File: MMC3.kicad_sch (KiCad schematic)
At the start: 18 parts, among them U11 NES-MMC3, U9 IS62C256AL-45TLI

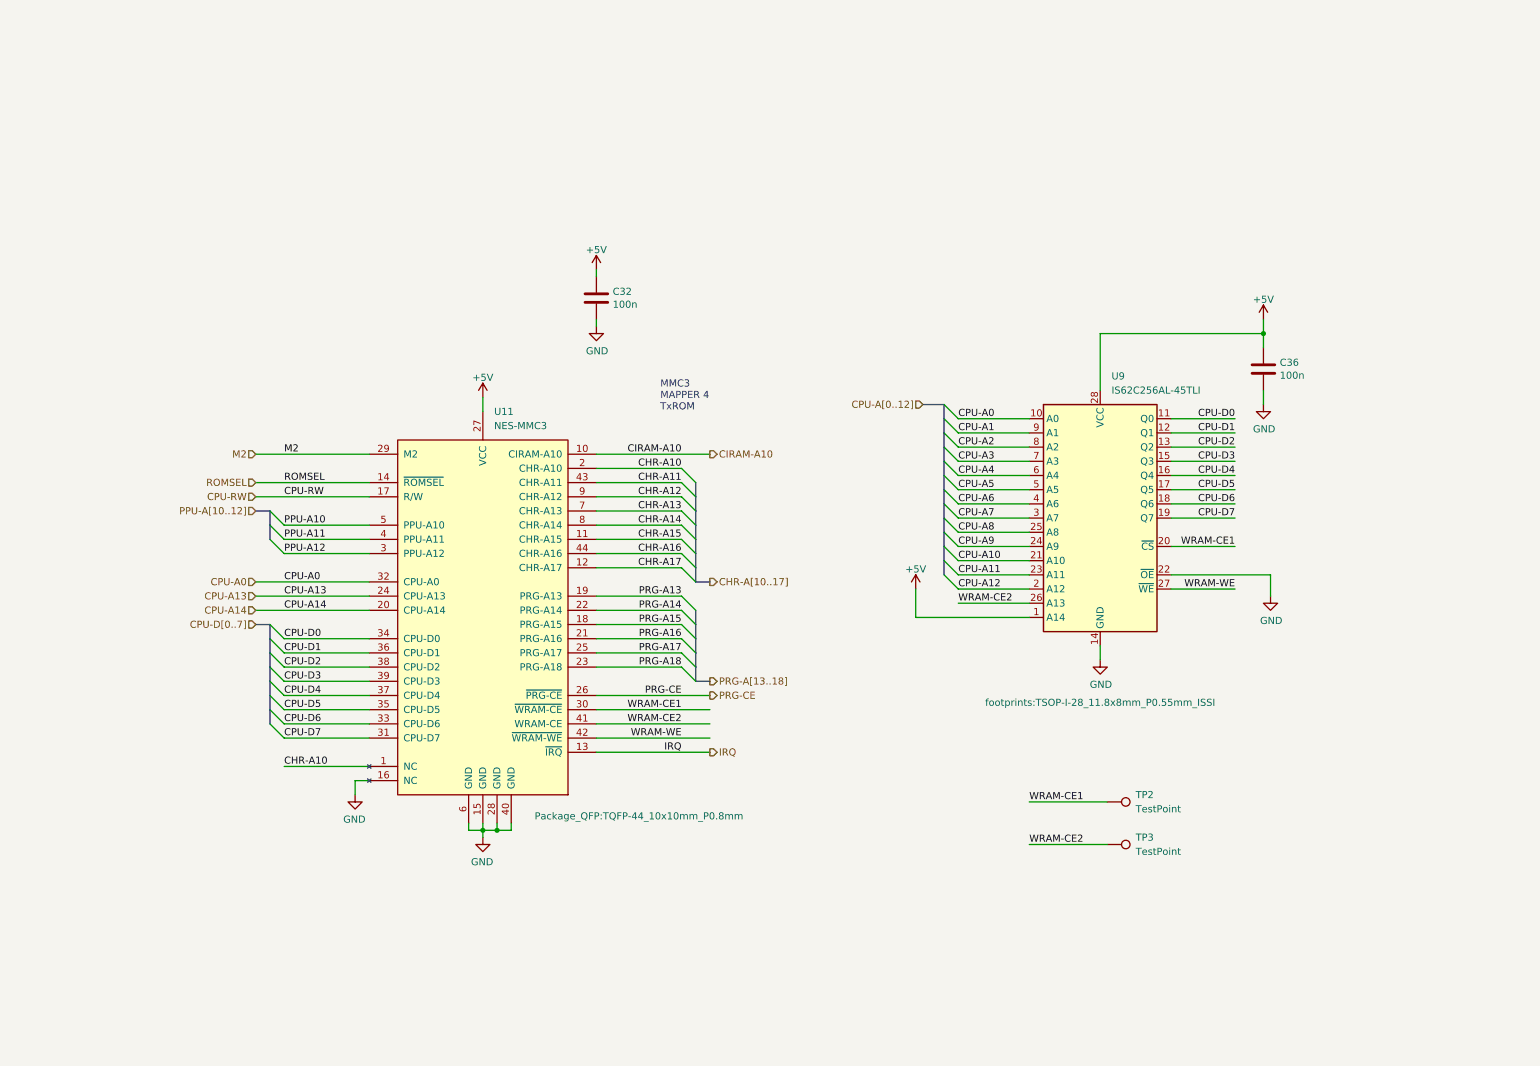
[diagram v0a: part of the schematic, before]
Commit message: rev2 sent to fab
Added CHR RAM.
Changed board to 4 layers (was 2 layers).
Changed passives to 0603 (was 0402)
Fixed CIRAM-A10 not being hooked up
Fixed PPU-A10..A12 being hooked to VRAM but should have been.
Added more silkscreen for easier debugging.
Added filter inductor to 5V from USB-C.
Changed video out to stock (was THS7374)
Changed audio circuit to stock (was headphone amp IC)
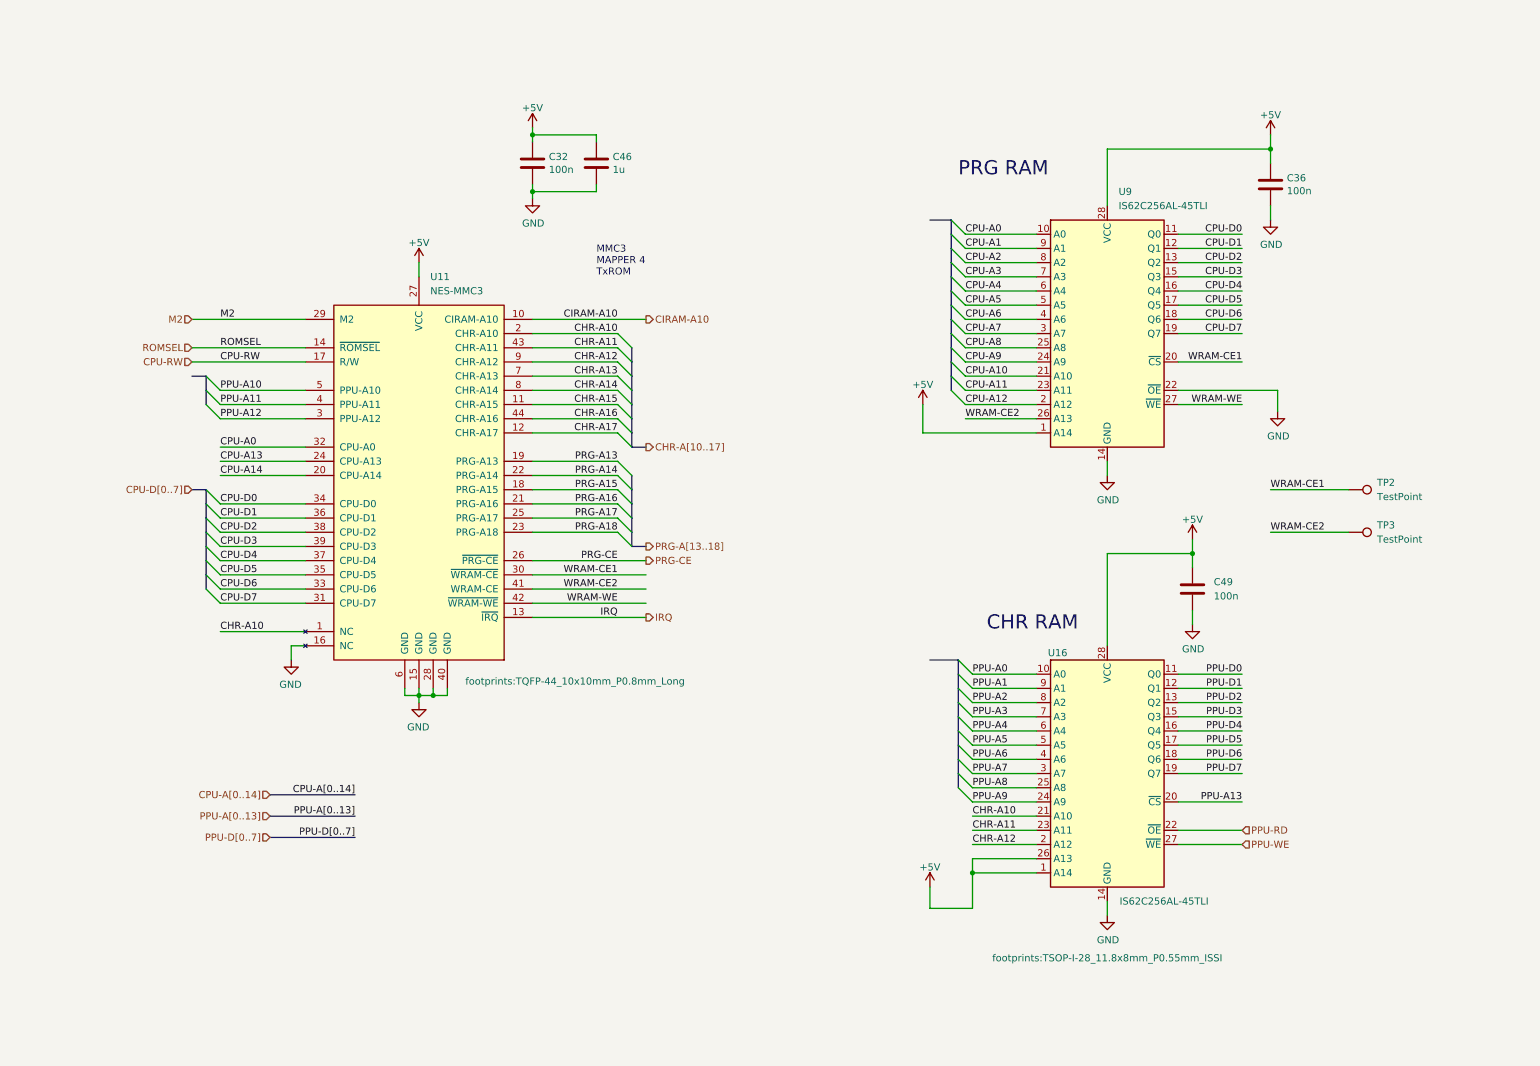
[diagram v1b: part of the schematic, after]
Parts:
- added C46: 1u, Capacitor_SMD:C_0603_1608Metric_Pad1.08x0.95mm_HandSolder, symbol Device:C
- added C49: 100n, Capacitor_SMD:C_0603_1608Metric_Pad1.08x0.95mm_HandSolder, symbol Device:C
- added U16: IS62C256AL-45TLI, footprints:TSOP-I-28_11.8x8mm_P0.55mm_ISSI, symbol Memory_RAM:KM62256CLP
- C32, C36: footprint Capacitor_SMD:C_0402_1005Metric -> Capacitor_SMD:C_0603_1608Metric_Pad1.08x0.95mm_HandSolder; Digikey 1276-1509-2-ND -> (none); MPN CL05B104KO5NNWC -> (none); QOH 10000 -> (none)
- U11: footprint Package_QFP:TQFP-44_10x10mm_P0.8mm -> footprints:TQFP-44_10x10mm_P0.8mm_Long
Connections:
- net +5V: now also C46.2, C49.2, U16.1 (A14), U16.26 (A13), U16.28 (VCC)
- net CHR-A10: now also U16.21 (A10)
- net CHR-A11: now also U16.23 (A11)
- net CHR-A12: now also U16.2 (A12)
- net GND: now also C46.1, C49.1, U16.14 (GND)
- net PPU-A13: now also U16.20 (~{CS})
- new net PPU-A0: U16.10 (A0)
- new net PPU-A1: U16.9 (A1)
- new net PPU-A2: U16.8 (A2)
- new net PPU-A3: U16.7 (A3)
- new net PPU-A4: U16.6 (A4)
- new net PPU-A5: U16.5 (A5)
- new net PPU-A6: U16.4 (A6)
- new net PPU-A7: U16.3 (A7)
- new net PPU-A8: U16.25 (A8)
- new net PPU-A9: U16.24 (A9)
- new net PPU-D0: U16.11 (Q0)
- new net PPU-D1: U16.12 (Q1)
- new net PPU-D2: U16.13 (Q2)
- new net PPU-D3: U16.15 (Q3)
- new net PPU-D4: U16.16 (Q4)
- new net PPU-D5: U16.17 (Q5)
- new net PPU-D6: U16.18 (Q6)
- new net PPU-D7: U16.19 (Q7)
- new net PPU-RD: U16.22 (~{OE})
- new net PPU-WE: U16.27 (~{WE})
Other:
- note added: "CHR RAM"
- note added: "PRG RAM"
- moved on the sheet: C32, C36, TP2, TP3, U11, U9

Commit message: filled out BOM
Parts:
- C32, C36, C49: Digikey (none) -> 1276-CL10B104KB8WPNDCT-ND; MPN (none) -> CL10B104KB8WPND
- C46: Digikey (none) -> 1276-1102-1-ND; MPN (none) -> CL10A105KA8NNNC
- TP2, TP3: now left out of the parts list
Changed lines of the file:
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@@
   (title_block
     (title "InGame-NES MMC3")
-    (date "2022-06-03")
-    (rev "1")
+    (date "2022-08-02")
+    (rev "2")
     (company "Late to the Game")
   )
@@
       (effects (font (size 1.27 1.27)) hide)
     )
-    (property "Description" "CAP CER 0.1UF 16V X7R 0402" (id 4) (at 100.33 25.4 0)
+    (property "Description" "CAP CER 0.1UF 50V X7R 0603" (id 4) (at 100.33 25.4 0)
       (effects (font (size 1.27 1.27)) hide)
     )
@@
       (effects (font (size 1.27 1.27)) hide)
     )
-    (property "Digikey" "" (id 6) (at 100.33 25.4 0)
+    (property "Digikey" "1276-CL10B104KB8WPNDCT-ND" (id 6) (at 100.33 25.4 0)
       (effects (font (size 1.27 1.27)) hide)
     )
-    (property "MPN" "" (id 7) (at 100.33 25.4 0)
+    (property "MPN" "CL10B104KB8WPND" (id 7) (at 100.33 25.4 0)
       (effects (font (size 1.27 1.27)) hide)
     )
@@
   )
   (symbol (lib_id "Connector:TestPoint") (at 246.38 83.82 270) (unit 1)
-    (in_bom yes) (on_board yes) (fields_autoplaced)
+    (in_bom no) (on_board yes) (fields_autoplaced)
     (property "Reference" "TP2" (id 0) (at 251.46 82.5499 90)
       (effects (font (size 1.27 1.27)) (justify left))
@@
       (effects (font (size 1.27 1.27)) hide)
     )
-    (property "Description" "CAP CER 0.1UF 16V X7R 0402" (id 4) (at 232.41 29.21 0)
+    (property "Description" "CAP CER 0.1UF 50V X7R 0603" (id 4) (at 232.41 29.21 0)
       (effects (font (size 1.27 1.27)) hide)
     )
@@
       (effects (font (size 1.27 1.27)) hide)
     )
-    (property "Digikey" "" (id 6) (at 232.41 29.21 0)
+    (property "Digikey" "1276-CL10B104KB8WPNDCT-ND" (id 6) (at 232.41 29.21 0)
       (effects (font (size 1.27 1.27)) hide)
     )
-    (property "MPN" "" (id 7) (at 232.41 29.21 0)
+    (property "MPN" "CL10B104KB8WPND" (id 7) (at 232.41 29.21 0)
       (effects (font (size 1.27 1.27)) hide)
     )
@@
       (effects (font (size 1.27 1.27)) hide)
     )
-    (property "Description" "CAP CER 0.1UF 16V X7R 0402" (id 4) (at 218.44 101.6 0)
+    (property "Description" "CAP CER 0.1UF 50V X7R 0603" (id 4) (at 218.44 101.6 0)
       (effects (font (size 1.27 1.27)) hide)
     )
@@
       (effects (font (size 1.27 1.27)) hide)
     )
-    (property "Digikey" "" (id 6) (at 218.44 101.6 0)
+    (property "Digikey" "1276-CL10B104KB8WPNDCT-ND" (id 6) (at 218.44 101.6 0)
       (effects (font (size 1.27 1.27)) hide)
     )
-    (property "MPN" "" (id 7) (at 218.44 101.6 0)
+    (property "MPN" "CL10B104KB8WPND" (id 7) (at 218.44 101.6 0)
       (effects (font (size 1.27 1.27)) hide)
     )
@@
       (effects (font (size 1.27 1.27)) hide)
     )
-    (property "Description" "CAP CER 1UF 25V X7R 0603" (id 4) (at 111.76 25.4 0)
+    (property "Description" "CAP CER 1UF 25V X5R 0603" (id 4) (at 111.76 25.4 0)
       (effects (font (size 1.27 1.27)) hide)
     )
@@
       (effects (font (size 1.27 1.27)) hide)
     )
-    (property "Digikey" "" (id 6) (at 111.76 25.4 0)
+    (property "Digikey" "1276-1102-1-ND" (id 6) (at 111.76 25.4 0)
       (effects (font (size 1.27 1.27)) hide)
     )
-    (property "MPN" "" (id 7) (at 111.76 25.4 0)
+    (property "MPN" "CL10A105KA8NNNC" (id 7) (at 111.76 25.4 0)
       (effects (font (size 1.27 1.27)) hide)
     )
@@
   )
   (symbol (lib_id "Connector:TestPoint") (at 246.38 91.44 270) (unit 1)
-    (in_bom yes) (on_board yes) (fields_autoplaced)
+    (in_bom no) (on_board yes) (fields_autoplaced)
     (property "Reference" "TP3" (id 0) (at 251.46 90.1699 90)
       (effects (font (size 1.27 1.27)) (justify left))
